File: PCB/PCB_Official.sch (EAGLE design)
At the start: 106 parts, among them IC1 MCP73871, J3 455-1750-1-ND, Q1 220mA/50V/3.5Ω, U1 TPS63070, U2 STM32F767ZIT6, U3 STM32L053C8T6, U4 TPS63070, U5 BATTERY-MANAGEMENT-TEMP_BQ274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

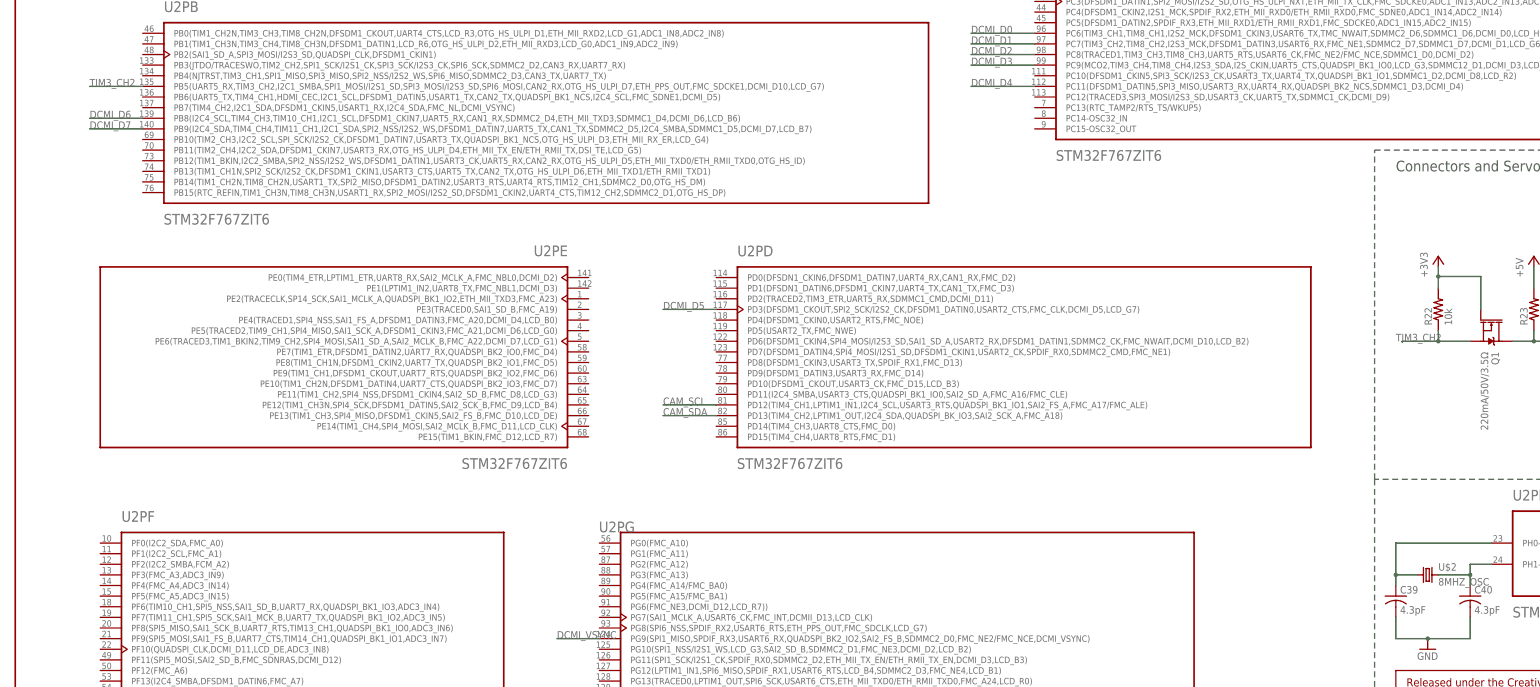
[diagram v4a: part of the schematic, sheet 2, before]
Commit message: Added PCB pin assignments and routed camera connector.
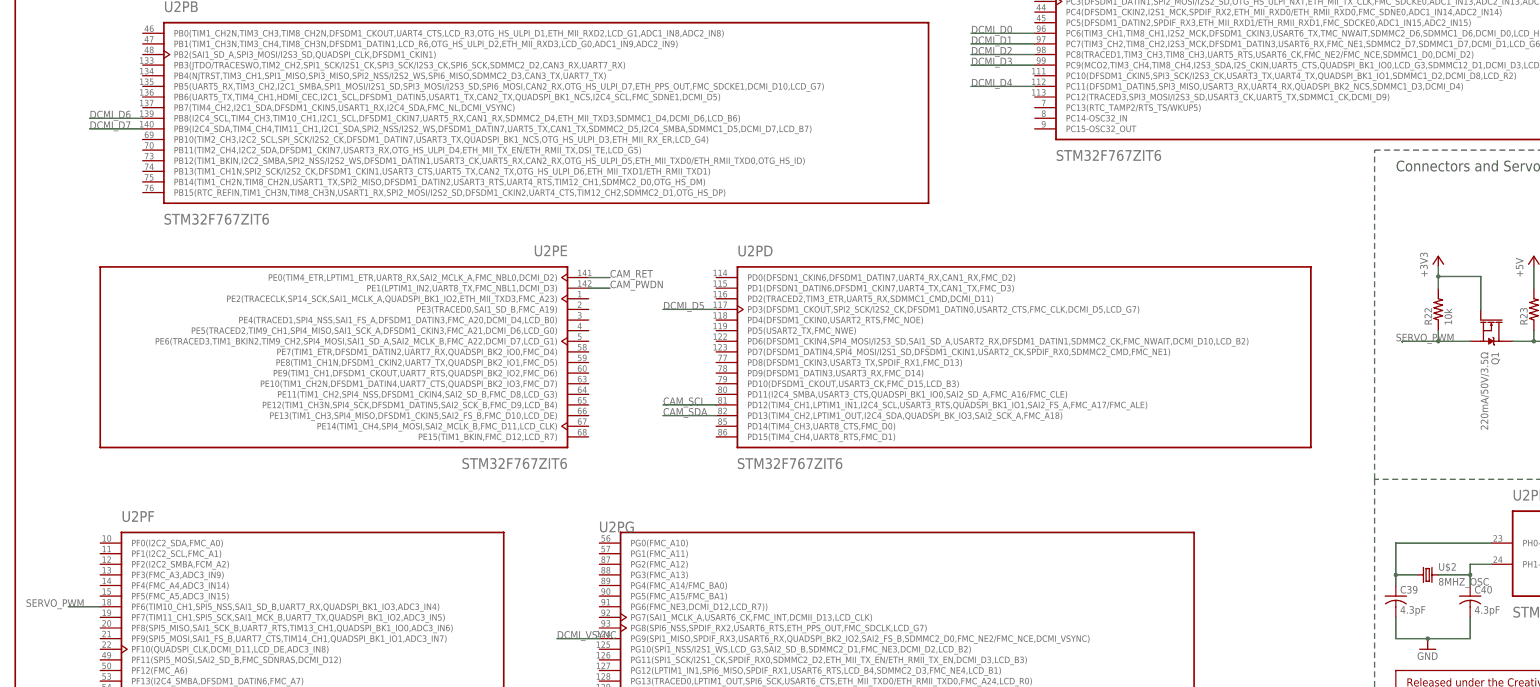
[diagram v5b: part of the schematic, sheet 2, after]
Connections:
- removed net TIM3_CH2: Q1.S, R22.1, U2PB.PB5(UART5_RX,TIM3_CH2,I2C1_SMBA,SPI1_MOSI/I2S1_SD,SPI3_MOSI/I2S3_SD,SPI6_MOSI,CAN2_RX,OTG_HS_ULPI_D7,ETH_PPS_OUT,FMC_SDCKE1,DCMI_D10,LCD_G7)
- new net SERVO_PWM: Q1.S, R22.1, U2PF.PF6(TIM10_CH1,SPI5_NSS,SAI1_SD_B,UART7_RX,QUADSPI_BK1_IO3,ADC3_IN4)
- net CAM_PWDN: now also U2PE.PE1(LPTIM1_IN2,UART8_TX,FMC_NBL1,DCMI_D3)
- net CAM_RET: now also U2PE.PE0(TIM4_ETR,LPTIM1_ETR,UART8_RX,SAI2_MCLK_A,FMC_NBL0,DCMI_D2)
- net LORA_RST: now also U3.PA10
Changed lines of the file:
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@@
 <?xml version="1.0" encoding="utf-8"?>
 <!DOCTYPE eagle SYSTEM "eagle.dtd">
-<eagle version="9.5.1">
+<eagle version="9.3.0">
 <drawing>
 <settings>
@@
 </segment>
 </net>
-<net name="TIM3_CH2" class="0">
-<segment>
-<pinref part="R22" gate="G$1" pin="1"/>
-<wire x1="340.36" y1="116.84" x2="340.36" y2="114.3" width="0.1524" layer="91"/>
-<pinref part="Q1" gate="NMOS" pin="S"/>
-<wire x1="340.36" y1="114.3" x2="347.98" y2="114.3" width="0.1524" layer="91"/>
-<wire x1="340.36" y1="114.3" x2="331.724" y2="114.3" width="0.1524" layer="91"/>
-<junction x="340.36" y="114.3"/>
-<wire x1="331.724" y1="114.046" x2="331.724" y2="114.3" width="0.1524" layer="91"/>
-<label x="330.2" y="114.3" size="1.778" layer="95"/>
-</segment>
-<segment>
-<pinref part="U2" gate="PB" pin="PB5(UART5_RX,TIM3_CH2,I2C1_SMBA,SPI1_MOSI/I2S1_SD,SPI3_MOSI/I2S3_SD,SPI6_MOSI,CAN2_RX,OTG_HS_ULPI_D7,ETH_PPS_OUT,FMC_SDCKE1,DCMI_D10,LCD_G7)"/>
-<wire x1="30.48" y1="175.26" x2="17.78" y2="175.26" width="0.1524" layer="91"/>
-<label x="17.78" y="175.26" size="1.778" layer="95"/>
-</segment>
-</net>
 <net name="+3V3" class="0">
 <segment>
@@
 <label x="254" y="256.54" size="1.27" layer="95"/>
 </segment>
+<segment>
+<pinref part="U2" gate="PE" pin="PE0(TIM4_ETR,LPTIM1_ETR,UART8_RX,SAI2_MCLK_A,FMC_NBL0,DCMI_D2)"/>
+<wire x1="137.16" y1="129.54" x2="142.24" y2="129.54" width="0.1524" layer="91"/>
+<label x="142.24" y="129.54" size="1.778" layer="95"/>
+</segment>
 </net>
 <net name="CAM_PWDN" class="0">
@@
 <wire x1="274.32" y1="256.54" x2="287.02" y2="256.54" width="0.1524" layer="91"/>
 <label x="279.4" y="256.54" size="1.27" layer="95"/>
+</segment>
+<segment>
+<pinref part="U2" gate="PE" pin="PE1(LPTIM1_IN2,UART8_TX,FMC_NBL1,DCMI_D3)"/>
+<wire x1="137.16" y1="127" x2="142.24" y2="127" width="0.1524" layer="91"/>
+<label x="142.24" y="127" size="1.778" layer="95"/>
 </segment>
 </net>
@@
 <pinref part="R4" gate="G$1" pin="1"/>
 <wire x1="292.1" y1="248.92" x2="292.1" y2="243.84" width="0.1524" layer="91"/>
+</segment>
+</net>
+<net name="SERVO_PWM" class="0">
+<segment>
+<pinref part="U2" gate="PF" pin="PF6(TIM10_CH1,SPI5_NSS,SAI1_SD_B,UART7_RX,QUADSPI_BK1_IO3,ADC3_IN4)"/>
+<wire x1="20.32" y1="50.8" x2="12.7" y2="50.8" width="0.1524" layer="91"/>
+<label x="2.54" y="50.8" size="1.778" layer="95"/>
+</segment>
+<segment>
+<pinref part="R22" gate="G$1" pin="1"/>
+<wire x1="340.36" y1="116.84" x2="340.36" y2="114.3" width="0.1524" layer="91"/>
+<pinref part="Q1" gate="NMOS" pin="S"/>
+<wire x1="340.36" y1="114.3" x2="347.98" y2="114.3" width="0.1524" layer="91"/>
+<wire x1="340.36" y1="114.3" x2="331.724" y2="114.3" width="0.1524" layer="91"/>
+<junction x="340.36" y="114.3"/>
+<wire x1="331.724" y1="114.046" x2="331.724" y2="114.3" width="0.1524" layer="91"/>
+<label x="330.2" y="114.3" size="1.778" layer="95"/>
 </segment>
 </net>
@@
 <label x="254" y="152.4" size="1.778" layer="95"/>
 </segment>
-</net>
+<segment>
+<pinref part="U3" gate="G$1" pin="PA10"/>
+<wire x1="45.72" y1="127" x2="35.56" y2="127" width="0.1524" layer="91"/>
+<label x="33.02" y="127" size="1.778" layer="95"/>
+</segment>
+</net>

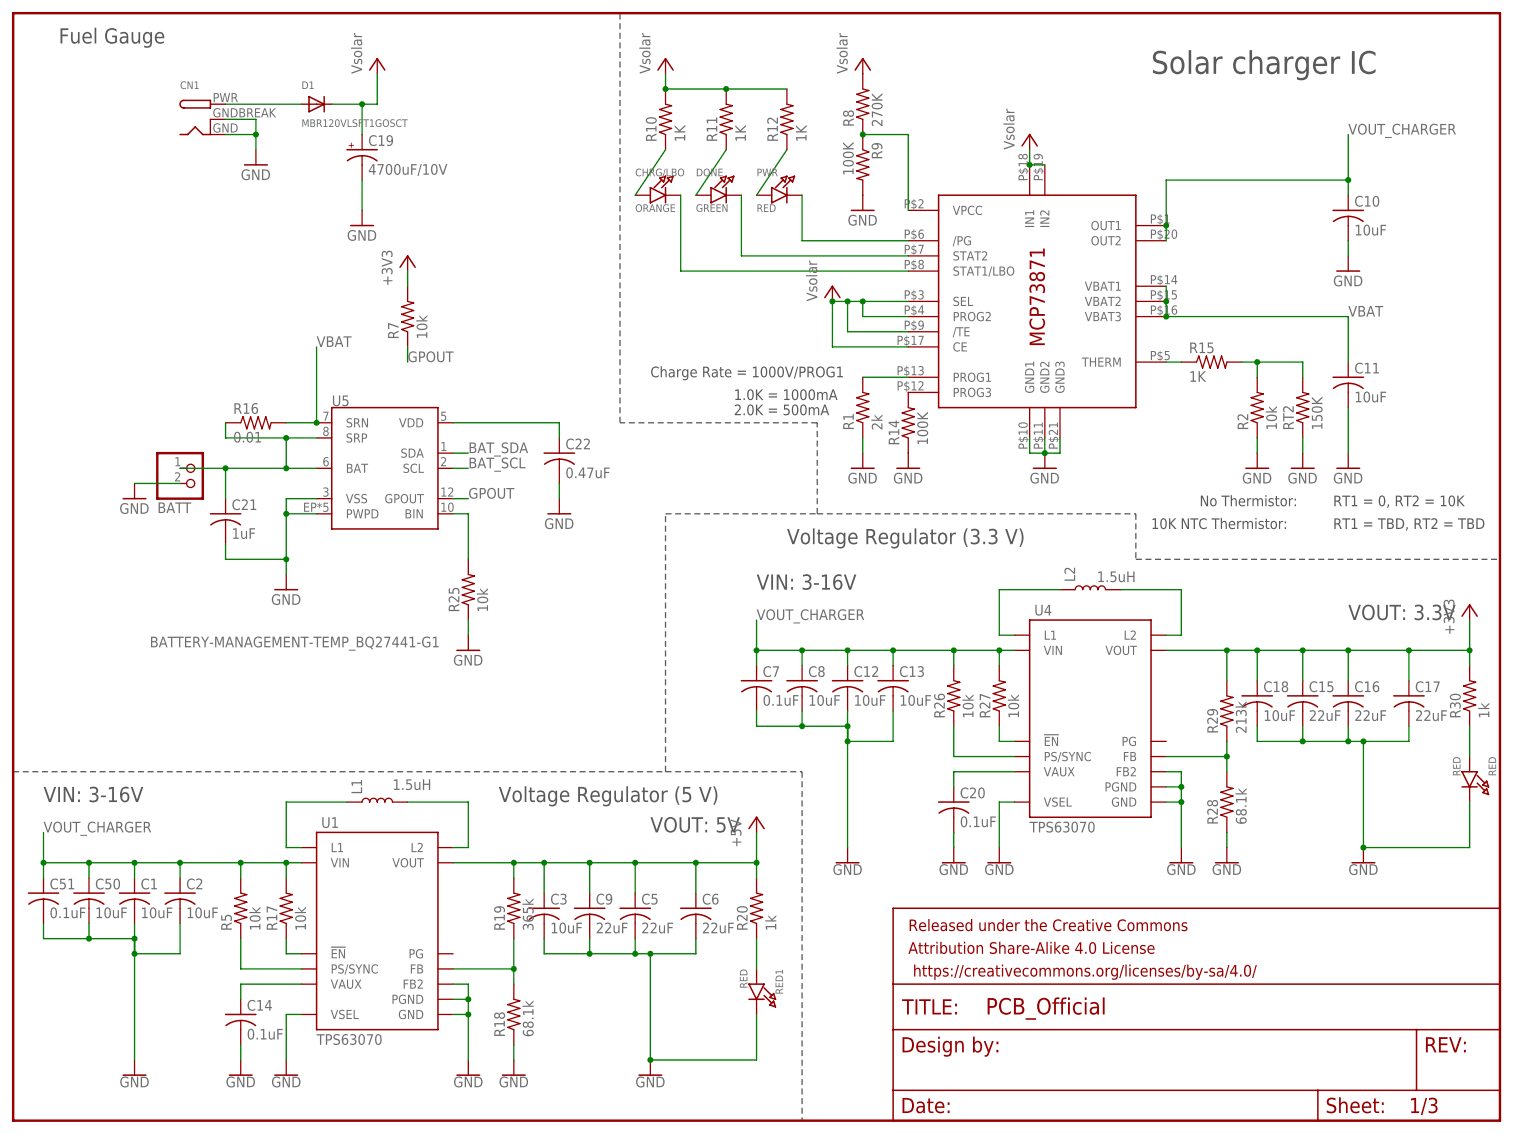
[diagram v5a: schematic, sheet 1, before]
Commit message: Corrected layout of 5V regulator, WIP for 3.3V regulator. Improved microcontroller layouts as well.
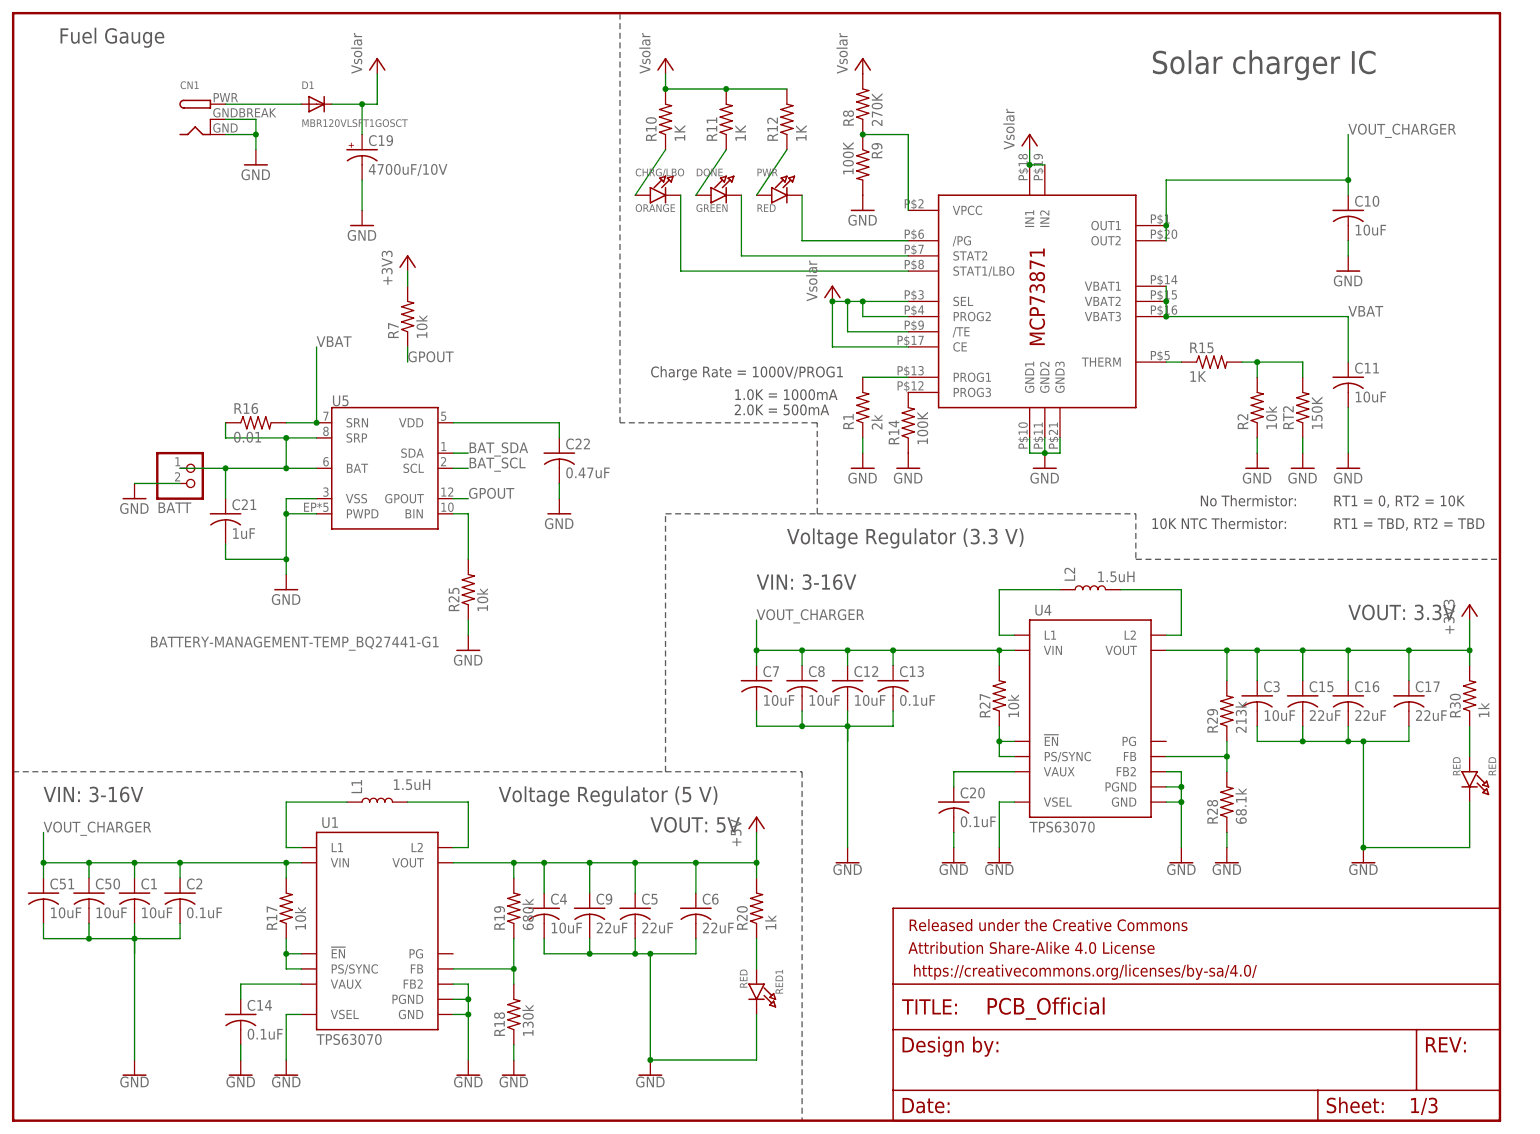
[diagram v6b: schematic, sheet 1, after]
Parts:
- removed C18: 10uF, adafruit:C-USC0805
- removed R26, R5: 10k, rcl:R-US_R0603
- added C4: 10uF, rcl:C-USC0603
- C13, C2: value 10uF -> 0.1uF
- C3: device adafruit:C-USC0805 -> rcl:C-USC0603
- C51, C7: value 0.1uF -> 10uF
- R18: value 68.1k -> 130k
- R19: value 365k -> 680k
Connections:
- removed net MCU_RST: J2.4, L0_PROGRAM.4, U2PWR_CONTR.NRST, U3.NRST
- removed net PS: R5.1, U1.PS/SYNC
- removed net PS1: R26.1, U4.PS/SYNC
- new net F7_RST: J2.4, U2PWR_CONTR.NRST
- new net L0_RST: L0_PROGRAM.4, U3.NRST
- net !EN: now also U1.PS/SYNC
- net !EN1: now also U4.PS/SYNC
- net +3V3: now also C3.1; no longer C18.1
- net +5V: now also C4.1; no longer C3.1
- net GND: now also C4.2; no longer C18.2
- net VOUT_CHARGER: no longer R26.2, R5.2
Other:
- moved on the sheet: C3
